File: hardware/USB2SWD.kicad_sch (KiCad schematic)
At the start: 22 parts, among them J1 USB_C_Receptacle_USB2.0_16P, SW1 SW_SPDT, SW2 SW_Push, U1 STM32F103C8Tx, U2 USBLC6-2P6, U3 FT232RL, Y1 Crystal

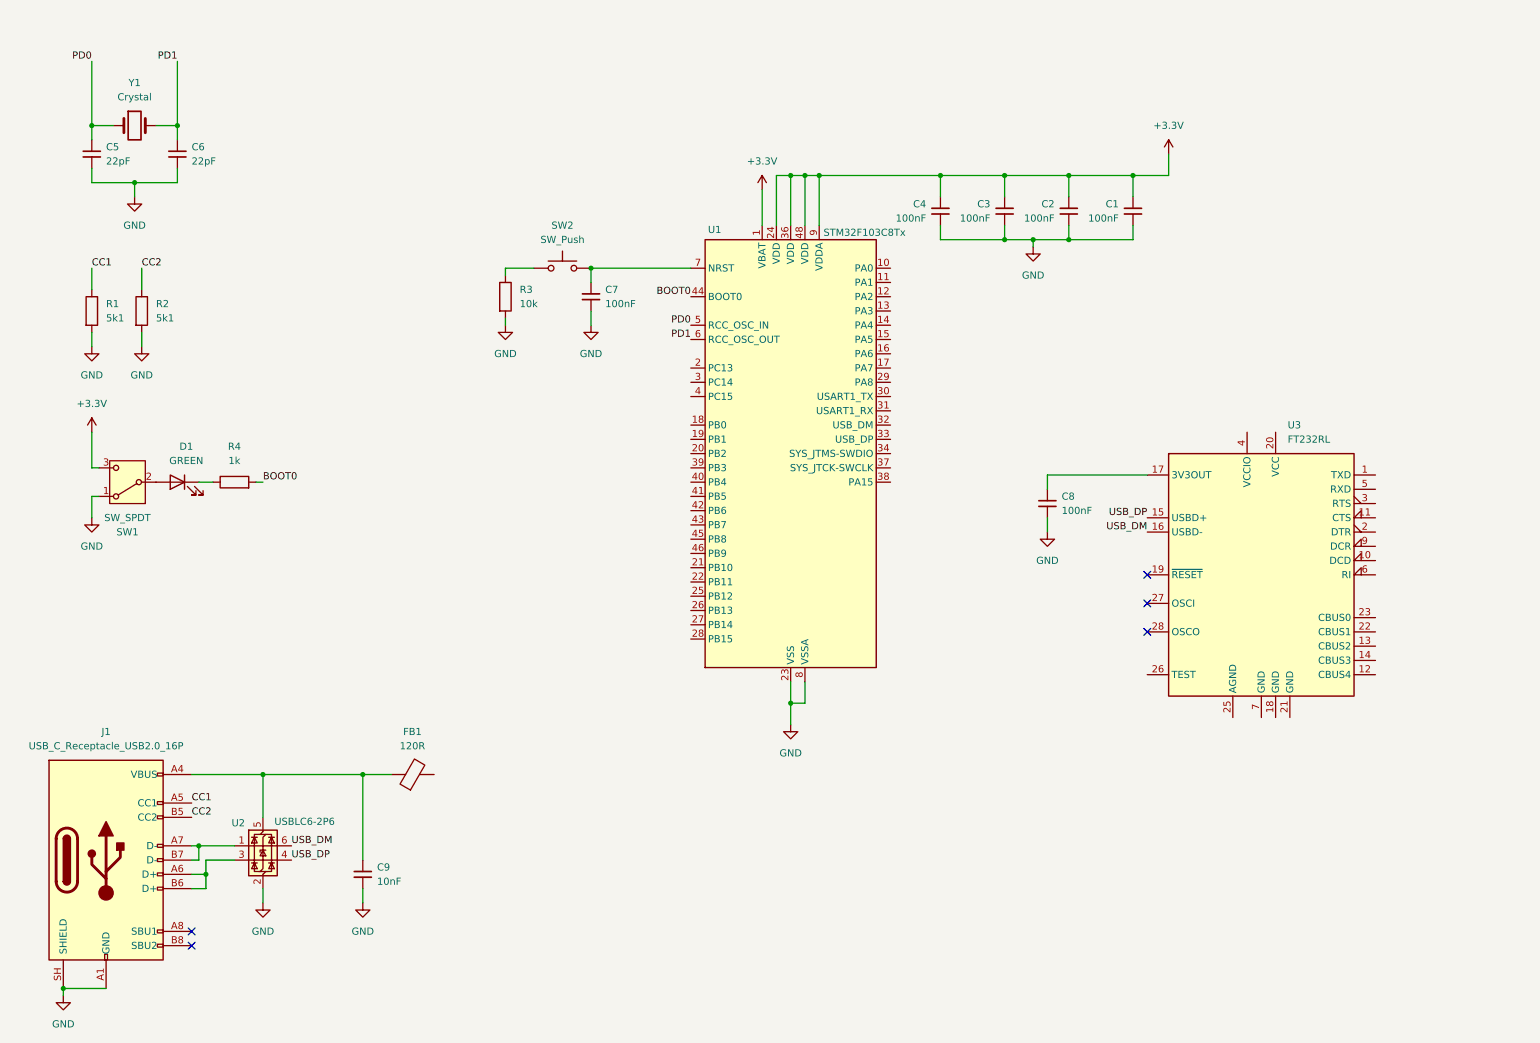
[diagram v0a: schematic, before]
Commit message: Add 32MB Flash and LDO
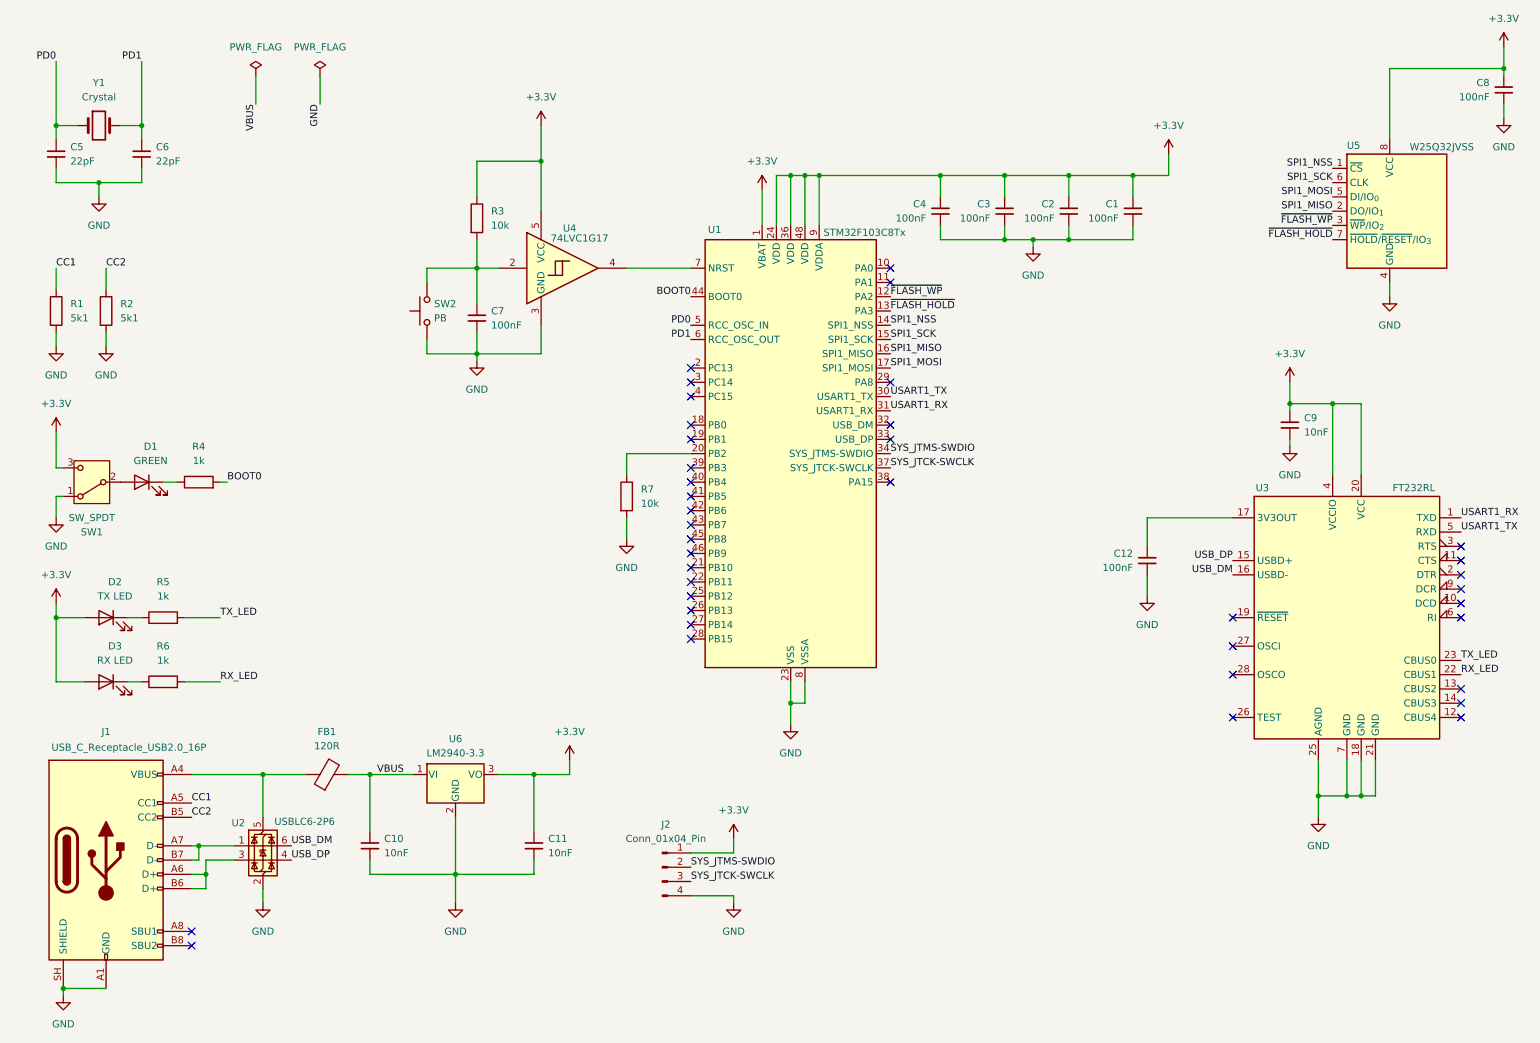
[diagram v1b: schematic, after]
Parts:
- added C10, C11: 10nF, Capacitor_SMD:C_0805_2012Metric_Pad1.18x1.45mm_HandSolder, symbol Device:C_Small
- added C12: 100nF, Capacitor_SMD:C_0805_2012Metric_Pad1.18x1.45mm_HandSolder, symbol Device:C_Small
- added D2: TX LED, LED_SMD:LED_0805_2012Metric_Pad1.15x1.40mm_HandSolder, symbol Device:LED
- added D3: RX LED, LED_SMD:LED_0805_2012Metric_Pad1.15x1.40mm_HandSolder, symbol Device:LED
- added J2: Conn_01x04_Pin, Connector_PinHeader_2.54mm:PinHeader_1x04_P2.54mm_Vertical, symbol Connector:Conn_01x04_Pin
- added R5, R6: 1k, Resistor_SMD:R_0805_2012Metric_Pad1.20x1.40mm_HandSolder, symbol Device:R
- added R7: 10k, Resistor_SMD:R_0805_2012Metric_Pad1.20x1.40mm_HandSolder, symbol Device:R
- added U4: 74LVC1G17, Package_TO_SOT_SMD:SOT-23-5_HandSoldering, symbol 74xGxx:74LVC1G17
- added U5: W25Q32JVSS, Package_SO:SOIC-8_5.3x5.3mm_P1.27mm, symbol Memory_Flash:W25Q32JVSS
- added U6: LM2940-3.3, Package_TO_SOT_SMD:SOT-223-3_TabPin2, symbol custom_symbols:LM2940-3.3
- SW2: value SW_Push -> PB
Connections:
- net +3.3V: now also C8.1, C9.1, R3.1, U3.20 (VCC), U3.4 (VCCIO), C11.1, D2.2 (A), D3.2 (A), J2.1 (Pin_1), U4.5 (VCC), U5.8 (VCC), U6.3 (VO)
- net GND: now also SW2.1, U3.18 (GND), U3.21 (GND), U3.25 (AGND), U3.7 (GND), C10.2, C11.2, C12.2, J2.4 (Pin_4), R7.2, U4.3 (GND), U5.4 (GND), U6.2 (GND); no longer R3.2
- net at FB1.1, J1.A4 (VBUS), J1.A9 (VBUS)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: no longer C9.1
- net USART1_RX: now reaches U3.1 (TXD)
- net USART1_RX: now also U1.31 (PA10)
- net at U3.17 (3V3OUT): now also C12.1; no longer C8.1
- net RX_LED: now reaches U3.22 (CBUS1)
- net RX_LED: now also R6.2
- net TX_LED: now reaches U3.23 (CBUS0)
- net TX_LED: now also R5.2
- net USART1_TX: now reaches U3.5 (RXD)
- net USART1_TX: now also U1.30 (PA9)
- net at C7.1, SW2.2: now also R3.2, U4.2; no longer U1.7 (NRST)
- net VBUS: now reaches FB1.2
- net VBUS: now also C10.1, U6.1 (VI)
- net ~{FLASH_WP}: now reaches U1.12 (PA2)
- net ~{FLASH_WP}: now also U5.3 (~{WP}/IO_{2})
- net ~{FLASH_HOLD}: now reaches U1.13 (PA3)
- net ~{FLASH_HOLD}: now also U5.7 (~{HOLD}/~{RESET}/IO_{3})
- net SPI1_NSS: now reaches U1.14 (PA4)
- net SPI1_NSS: now also U5.1 (~{CS})
- net SPI1_SCK: now reaches U1.15 (PA5)
- net SPI1_SCK: now also U5.6 (CLK)
- net SPI1_MISO: now reaches U1.16 (PA6)
- net SPI1_MISO: now also U5.2 (DO/IO_{1})
- net SPI1_MOSI: now reaches U1.17 (PA7)
- net SPI1_MOSI: now also U5.5 (DI/IO_{0})
- net at U1.20 (PB2): now also R7.1
- net SYS_JTMS-SWDIO: now reaches U1.34 (PA13)
- net SYS_JTMS-SWDIO: now also J2.2 (Pin_2)
- net SYS_JTCK-SWCLK: now reaches U1.37 (PA14)
- net SYS_JTCK-SWCLK: now also J2.3 (Pin_3)
- new net: D3.1 (K), R6.1
- new net: D2.1 (K), R5.1
- new net: U1.7 (NRST), U4.4
- no-connect marks 5 -> 39
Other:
- company: (none) -> Zadock Maloba Muyeshi
- title: (none) -> OpenBoardLink (USB2SWD)
- moved on the sheet: C5, C6, D1, FB1, R1, R2, R4, SW1, U3, Y1

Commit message: Fix all ERC errors
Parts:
- removed D1: GREEN, LED_SMD:LED_0805_2012Metric_Pad1.15x1.40mm_HandSolder, symbol Device:LED
- added R8: 100R, Resistor_SMD:R_0805_2012Metric_Pad1.20x1.40mm_HandSolder, symbol Device:R
- R4: value 1k -> 10k
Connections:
- net +3.3V: no longer J2.1 (Pin_1)
- net GND: no longer J2.4 (Pin_4)
- net at SW1.2 (B): now also R4.1
- net T_NRST: now reaches U1.18 (PB0)
- net T_NRST: now also J2.3 (Pin_3)
- net T_SWDCLK: now reaches U1.26 (PB13)
- net T_SWDCLK: now also J2.1 (Pin_1)
- net T_SWDIO: now reaches U1.27 (PB14)
- net T_SWDIO: now also J2.2 (Pin_2), R8.1
- net SWDIO_IN: now reaches U1.28 (PB15)
- net SWDIO_IN: now also R8.2
- net T_SWO: now reaches U1.38 (PA15)
- net T_SWO: now also J2.4 (Pin_4)
- net SYS_JTCK-SWCLK: no longer names the net of U1.37 (PA14)
- net SYS_JTCK-SWCLK: no longer J2.3 (Pin_3)
- net SYS_JTMS-SWDIO: no longer names the net of U1.34 (PA13)
- net SYS_JTMS-SWDIO: no longer J2.2 (Pin_2)
- no-connect marks 39 -> 36
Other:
- moved on the sheet: R4

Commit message: Rev-1 v0.1
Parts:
- removed J2: Conn_01x04_Pin, Connector_PinHeader_2.54mm:PinHeader_1x04_P2.54mm_Vertical, symbol Connector:Conn_01x04_Pin
- removed U4: 74LVC1G17, Package_TO_SOT_SMD:SOT-23-5_HandSoldering, symbol 74xGxx:74LVC1G17
- removed U6: LM2940-3.3, Package_TO_SOT_SMD:SOT-223-3_TabPin2, symbol custom_symbols:LM2940-3.3
- added J2: Conn_01x06_Pin, Connector_PinHeader_2.54mm:PinHeader_1x06_P2.54mm_Vertical, symbol Connector:Conn_01x06_Pin
- added R10, R11, R15, R16, R9: 10k, Resistor_SMD:R_0805_2012Metric_Pad1.20x1.40mm_HandSolder, symbol Device:R
- added R12: 47R, Resistor_SMD:R_0805_2012Metric_Pad1.20x1.40mm_HandSolder, symbol Device:R
- added R13, R14: 1k, Resistor_SMD:R_0805_2012Metric_Pad1.20x1.40mm_HandSolder, symbol Device:R
- added U6: AP2112K-3.3, Package_TO_SOT_SMD:SOT-23-5, symbol Regulator_Linear:AP2112K-3.3
- R8: value 100R -> 330R
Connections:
- net +3.3V: now also R10.1, R11.1, R14.2, R15.1, R9.1, U6.5 (VOUT); no longer C9.1, U3.20 (VCC), U3.4 (VCCIO)
- net GND: now also J2.6 (Pin_6), R13.1, R16.2, U6.2 (GND)
- net SPI1_NSS: now also R11.2
- net T_NRST: now also U1.38 (PA15), J2.1 (Pin_1); no longer U1.18 (PB0)
- net T_SWDCLK: now also R12.2
- net T_SWDIO: now also J2.3 (Pin_3), R14.1
- net T_SWO: now also U1.22 (PB11), J2.4 (Pin_4); no longer U1.38 (PA15)
- net VBUS: now also C9.1, U3.20 (VCC), U3.4 (VCCIO), U6.1 (VIN), U6.3 (EN)
- net ~{FLASH_HOLD}: now also R10.2
- net ~{FLASH_WP}: now also R9.2
- net at C7.1, R3.2, SW2.2: now also U1.7 (NRST)
- new net T_SWDCLK_P: J2.2 (Pin_2), R12.1, R13.2
- new net VTREF: J2.5 (Pin_5), R15.2, R16.1, U1.18 (PB0)
- no-connect marks 36 -> 35
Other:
- moved on the sheet: C7, R3, SW2

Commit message: Rev-1 v0.2
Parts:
- removed U3: FT232RL, Package_SO:SSOP-28_5.3x10.2mm_P0.65mm, symbol Interface_USB:FT232RL
- added U3: CH340N, Package_SO:JEITA_SOIC-8_3.9x4.9mm_P1.27mm, symbol Interface_USB:CH340N
- renumbered U5 to U4, U6 to U5
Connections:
- net GND: now also U3.3 (GND)
- net USART1_RX: now also U3.6 (TXD)
- net USART1_TX: now also U3.7 (RXD)
- net USB_DM: now also U3.2 (UD-)
- net USB_DP: now also U3.1 (UD+)
- net VBUS: now also U3.5 (VCC)
- net at C12.1: now also U3.8 (V3)
- no-connect marks 35 -> 23

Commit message: Rev-1 v0.3
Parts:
- removed D3: RX LED, LED_SMD:LED_0805_2012Metric_Pad1.15x1.40mm_HandSolder, symbol Device:LED
- removed R6: 1k, Resistor_SMD:R_0805_2012Metric_Pad1.20x1.40mm_HandSolder, symbol Device:R
- D2: value TX LED -> PWR LED
- U3: LCSC (none) -> C2977777
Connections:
- net TX_LED is gone; now on net GND: R5.2
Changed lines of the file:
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@@
 	)
 	(junction
-		(at 20.32 121.92)
-		(diameter 0)
-		(color 0 0 0 0)
-	)
-	(junction
 		(at 200.66 54.61)
 		(diameter 0)
@@
 	(wire
 		(pts
-			(xy 43.18 133.35) (xy 49.53 133.35)
-		)
-		(stroke
-			(width 0)
-			(type default)
-		)
-	)
-	(wire
-		(pts
 			(xy 57.15 149.86) (xy 64.77 149.86)
 		)
@@
 	(wire
 		(pts
-			(xy 33.02 133.35) (xy 35.56 133.35)
-		)
-		(stroke
-			(width 0)
-			(type default)
-		)
-	)
-	(wire
-		(pts
 			(xy 44.45 170.18) (xy 46.99 170.18)
 		)
@@
 	(wire
 		(pts
-			(xy 20.32 133.35) (xy 20.32 121.92)
-		)
-		(stroke
-			(width 0)
-			(type default)
-		)
-	)
-	(wire
-		(pts
 			(xy 76.2 149.86) (xy 76.2 160.02)
 		)
@@
 	(wire
 		(pts
-			(xy 43.18 121.92) (xy 49.53 121.92)
+			(xy 43.18 121.92) (xy 50.8 121.92)
 		)
 		(stroke
@@
 	(wire
 		(pts
+			(xy 50.8 125.73) (xy 50.8 121.92)
+		)
+		(stroke
+			(width 0)
+			(type default)
+		)
+	)
+	(wire
+		(pts
 			(xy 200.66 52.07) (xy 200.66 54.61)
 		)
@@
 	(wire
 		(pts
-			(xy 25.4 133.35) (xy 20.32 133.35)
-		)
-		(stroke
-			(width 0)
-			(type default)
-		)
-	)
-	(wire
-		(pts
 			(xy 35.56 22.86) (xy 35.56 34.29)
 		)
@@
 		)
 	)
-	(label "STM_VCC"
-		(at 163.83 43.18 0)
-		(effects
-			(font
-				(size 1.27 1.27)
-			)
-			(justify left bottom)
-		)
-	)
 	(label "T_SWDIO"
 		(at 127 189.23 0)
@@
 		)
 	)
-	(label "TX_LED"
-		(at 49.53 121.92 0)
-		(effects
-			(font
-				(size 1.27 1.27)
-			)
-			(justify left bottom)
-		)
-	)
 	(label "SPI1_MOSI"
 		(at 168.91 77.47 0)
@@
 		)
 	)
-	(label "RX_LED"
-		(at 49.53 133.35 0)
-		(effects
-			(font
-				(size 1.27 1.27)
-			)
-			(justify left bottom)
-		)
-	)
 	(label "SPI1_MISO"
 		(at 168.91 74.93 0)
@@
 	)
 	(symbol
-		(lib_id "Device:R")
-		(at 39.37 133.35 90)
-		(unit 1)
-		(body_style 1)
-		(exclude_from_sim no)
-		(in_bom yes)
-		(on_board yes)
-		(in_pos_files yes)
-		(dnp no)
-		(fields_autoplaced yes)
-		(property "Reference" "R6"
-			(at 39.37 127 90)
-			(show_name no)
-			(do_not_autoplace no)
-			(effects
-				(font
-					(size 1.27 1.27)
-				)
-			)
-		)
-		(property "Value" "1k"
-			(at 39.37 129.54 90)
-			(show_name no)
-			(do_not_autoplace no)
-			(effects
-				(font
-					(size 1.27 1.27)
-				)
-			)
-		)
-		(property "Footprint" "Resistor_SMD:R_0805_2012Metric_Pad1.20x1.40mm_HandSolder"
-			(at 39.37 135.128 90)
-			(hide yes)
-			(show_name no)
-			(do_not_autoplace no)
-			(effects
-				(font
-					(size 1.27 1.27)
-				)
-			)
-		)
-		(property "Datasheet" ""
-			(at 39.37 133.35 0)
-			(hide yes)
-			(show_name no)
-			(do_not_autoplace no)
-			(effects
-				(font
-					(size 1.27 1.27)
-				)
-			)
-		)
-		(property "Description" "Resistor"
-			(at 39.37 133.35 0)
-			(hide yes)
-			(show_name no)
-			(do_not_autoplace no)
-			(effects
-				(font
-					(size 1.27 1.27)
-				)
-			)
-		)
-		(pin "2"
-		)
-		(pin "1"
-		)
-		(instances
-			(project "USB2SWD"
-				(path "/7bc2913b-0444-4f4b-915c-7d0fc0e0be92"
-					(reference "R6")
-					(unit 1)
-				)
-			)
-		)
-	)
-	(symbol
 		(lib_id "Connector:USB_C_Receptacle_USB2.0_16P")
 		(at 29.21 165.1 0)
@@
 			)
 		)
-		(property "Value" "TX LED"
+		(property "Value" "PWR LED"
 			(at 30.7975 118.11 0)
 			(show_name no)
@@
 	)
 	(symbol
-		(lib_id "Device:LED")
-		(at 29.21 133.35 0)
-		(mirror y)
-		(unit 1)
-		(body_style 1)
-		(exclude_from_sim no)
-		(in_bom yes)
-		(on_board yes)
-		(in_pos_files yes)
-		(dnp no)
-		(fields_autoplaced yes)
-		(property "Reference" "D3"
-			(at 30.7975 127 0)
-			(show_name no)
-			(do_not_autoplace no)
-			(effects
-				(font
-					(size 1.27 1.27)
-				)
-			)
-		)
-		(property "Value" "RX LED"
-			(at 30.7975 129.54 0)
-			(show_name no)
-			(do_not_autoplace no)
-			(effects
-				(font
-					(size 1.27 1.27)
-				)
-			)
-		)
-		(property "Footprint" "LED_SMD:LED_0805_2012Metric_Pad1.15x1.40mm_HandSolder"
-			(at 29.21 133.35 0)
-			(hide yes)
-			(show_name no)
-			(do_not_autoplace no)
-			(effects
-				(font
-					(size 1.27 1.27)
-				)
-			)
-		)
-		(property "Datasheet" ""
-			(at 29.21 133.35 0)
-			(hide yes)
-			(show_name no)
-			(do_not_autoplace no)
-			(effects
-				(font
-					(size 1.27 1.27)
-				)
-			)
-		)
-		(property "Description" "Light emitting diode"
-			(at 29.21 133.35 0)
-			(hide yes)
-			(show_name no)
-			(do_not_autoplace no)
-			(effects
-				(font
-					(size 1.27 1.27)
-				)
-			)
-		)
-		(property "Sim.Pins" "1=K 2=A"
-			(at 29.21 133.35 0)
-			(hide yes)
-			(show_name no)
-			(do_not_autoplace no)
-			(effects
-				(font
-					(size 1.27 1.27)
-				)
-			)
-		)
-		(pin "2"
-		)
-		(pin "1"
-		)
-		(instances
-			(project "USB2SWD"
-				(path "/7bc2913b-0444-4f4b-915c-7d0fc0e0be92"
-					(reference "D3")
-					(unit 1)
-				)
-			)
-		)
-	)
-	(symbol
 		(lib_id "power:+3.3V")
 		(at 127 177.8 0)
@@
 	)
 	(symbol
+		(lib_id "power:GND")
+		(at 50.8 125.73 0)
+		(unit 1)
+		(body_style 1)
+		(exclude_from_sim no)
+		(in_bom yes)
+		(on_board yes)
+		(in_pos_files yes)
+		(dnp no)
+		(fields_autoplaced yes)
+		(property "Reference" "#PWR033"
+			(at 50.8 132.08 0)
+			(hide yes)
+			(show_name no)
+			(do_not_autoplace no)
+			(effects
+				(font
+					(size 1.27 1.27)
+				)
+			)
+		)
+		(property "Value" "GND"
+			(at 50.8 130.81 0)
+			(show_name no)
+			(do_not_autoplace no)
+			(effects
+				(font
+					(size 1.27 1.27)
+				)
+			)
+		)
+		(property "Footprint" ""
+			(at 50.8 125.73 0)
+			(hide yes)
+			(show_name no)
+			(do_not_autoplace no)
+			(effects
+				(font
+					(size 1.27 1.27)
+				)
+			)
+		)
+		(property "Datasheet" ""
+			(at 50.8 125.73 0)
+			(hide yes)
+			(show_name no)
+			(do_not_autoplace no)
+			(effects
+				(font
+					(size 1.27 1.27)
+				)
+			)
+		)
+		(property "Description" "Power symbol creates a global label with name \"GND\" , ground"
+			(at 50.8 125.73 0)
+			(hide yes)
+			(show_name no)
+			(do_not_autoplace no)
+			(effects
+				(font
+					(size 1.27 1.27)
+				)
+			)
+		)
+		(pin "1"
+		)
+		(instances
+			(project "USB2SWD"
+				(path "/7bc2913b-0444-4f4b-915c-7d0fc0e0be92"
+					(reference "#PWR033")
+					(unit 1)
+				)
+			)
+		)
+	)
+	(symbol
 		(lib_id "Device:C_Small")
 		(at 278.13 27.94 0)
@@
 			(at 254 143.51 0)
 			(hide yes)
+			(show_name no)
+			(do_not_autoplace no)
+			(effects
+				(font
+					(size 1.27 1.27)
+				)
+			)
+		)
+		(property "LCSC" "C2977777"
+			(at 254 143.51 0)
+			(hide yes)
